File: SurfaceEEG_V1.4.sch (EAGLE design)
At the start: 69 parts, among them IC1 LMV602, IC2 TSZ124IQ4T, U1 MCP4442-103E/ST, U2 ATMEGA328P-MU

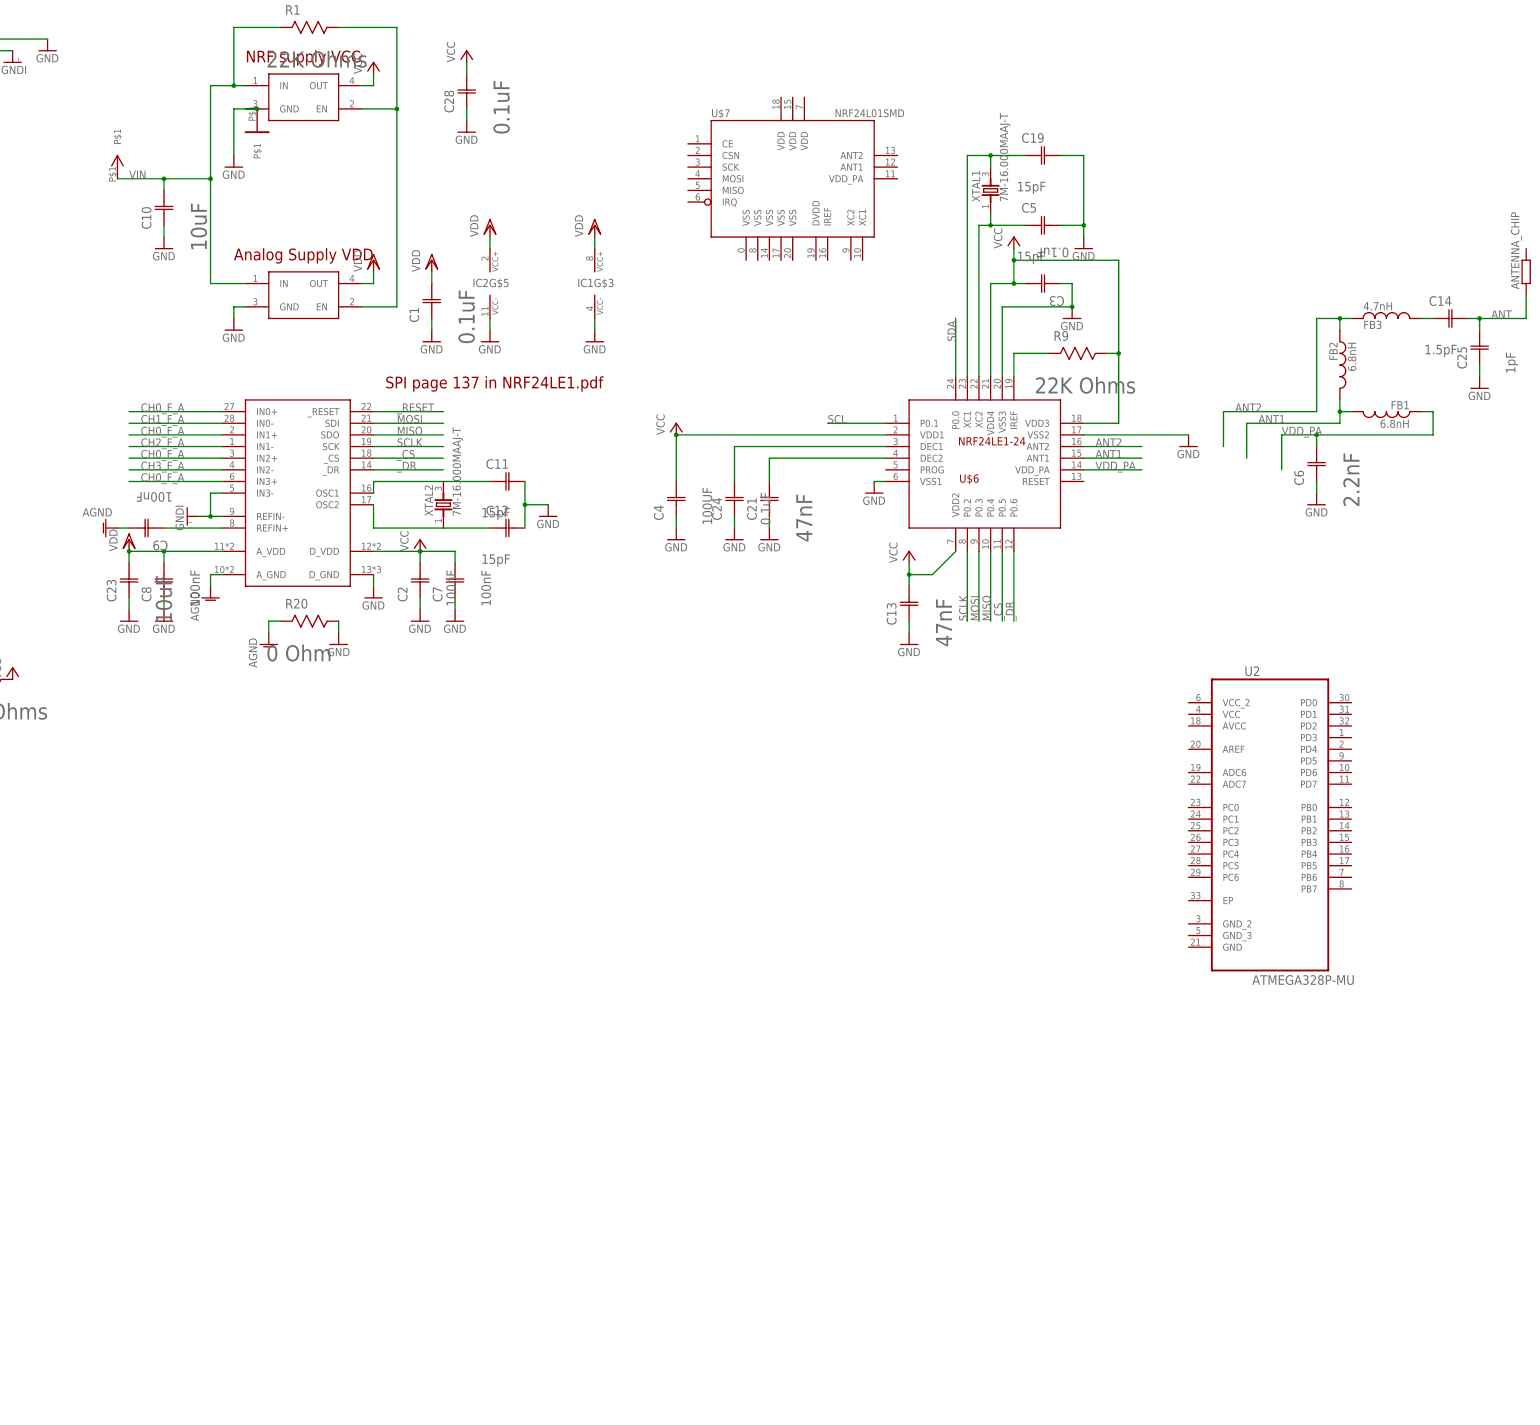
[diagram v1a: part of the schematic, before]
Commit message: Version 1.4 with atmega328 and hrf24L01 ready
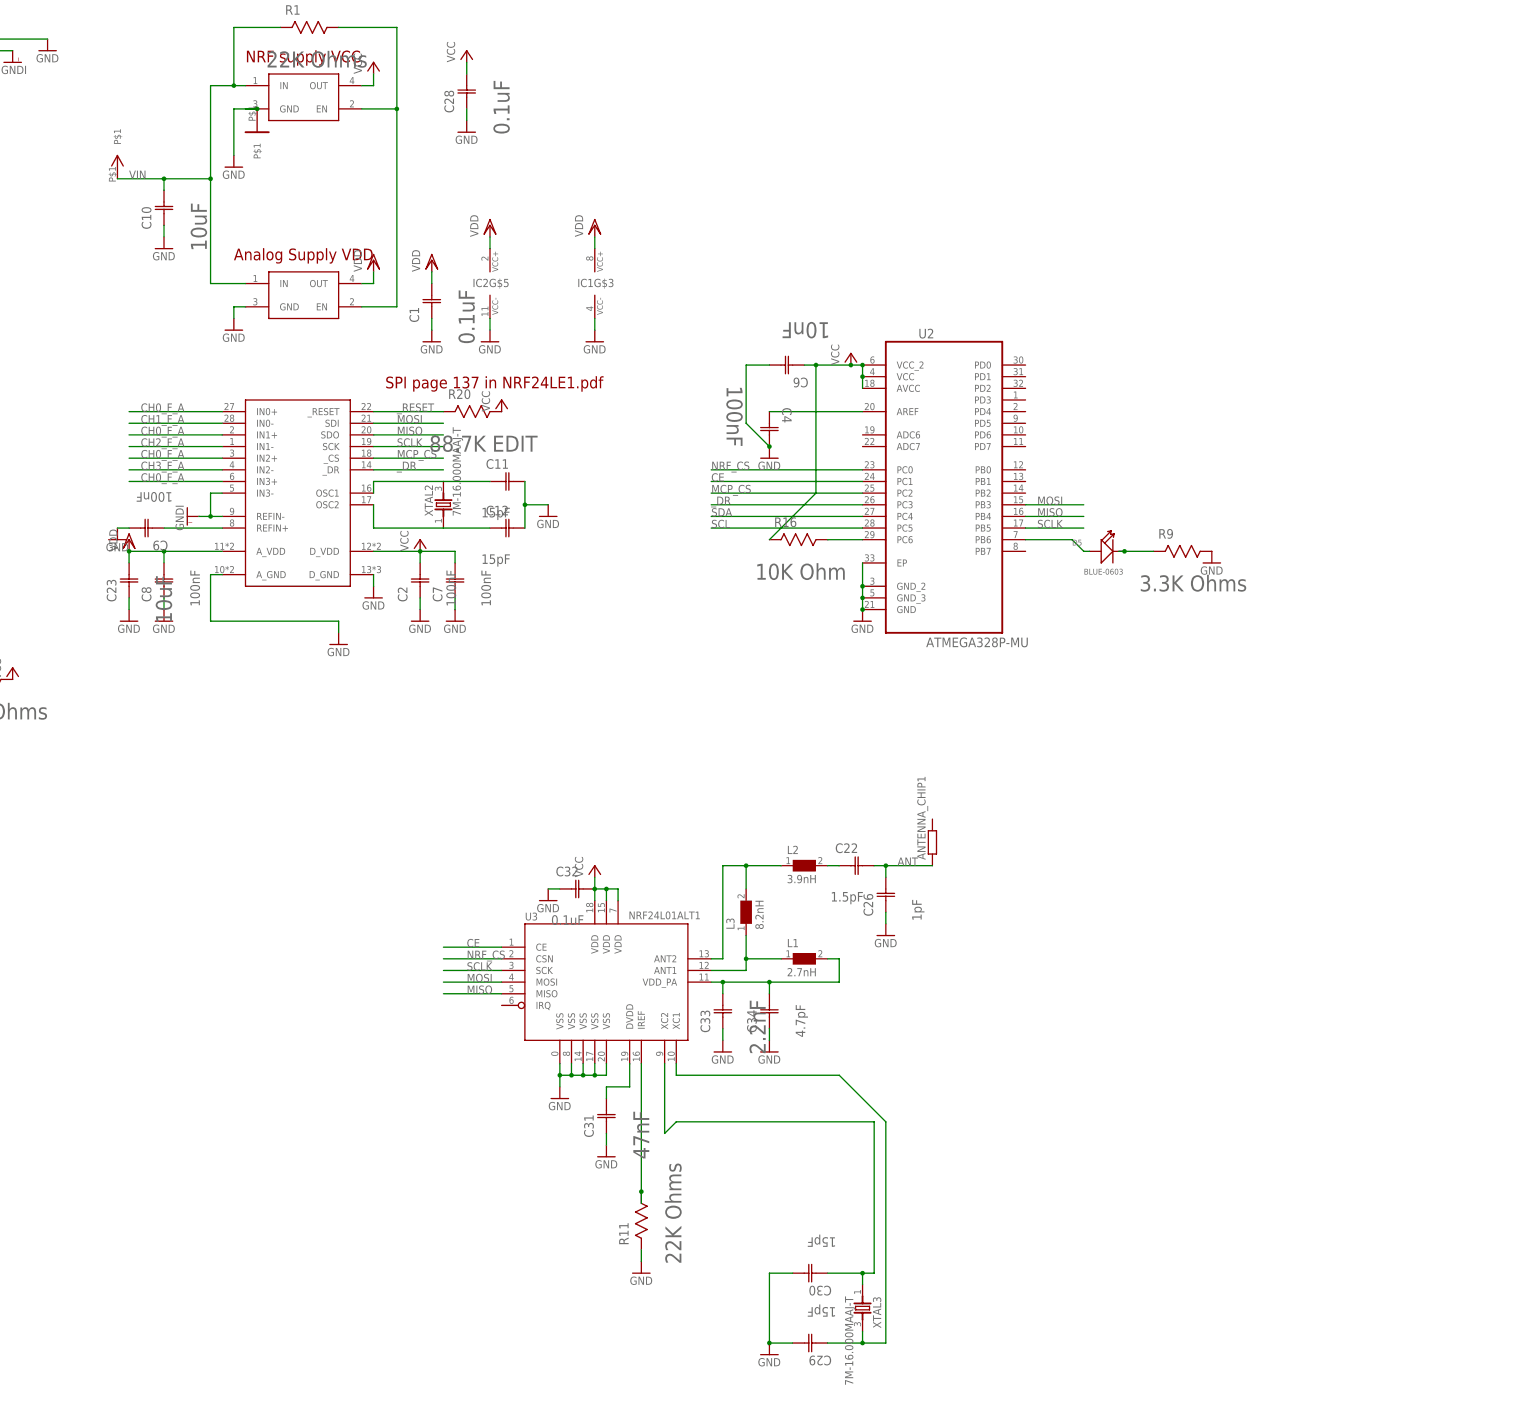
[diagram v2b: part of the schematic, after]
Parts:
- removed ANTENNA_CHIP: (no value), ELL-i-Passives:R0805
- removed C13, C21: 47nF, (manufact)-Kemet-element14:C0603C473K1RACTU
- removed C14: 1.5pF, (manufact)-capacitors-AVX-element14:UQCL2A1R5BAT2A/500
- removed C19, C5: 15pF, (manufact)-capacitors-AVX-element14:UQCL2A150JAT2A/500
- removed C24, C3: 0.1uF, (manufact)-capacitors-AVX-element14:04023C104KAT2A
- removed C25: 1pF, (manufact)-capacitors-AVX-element14:UQCL2A1R0BAT2A/500
- removed FB1, FB2: 6.8nH, ELL-i-Passives:FB0402
- removed FB3: 4.7nH, ELL-i-Passives:FB0402
- removed U$6: NRF24LE1-24, (misc)-parts-that-we-use:NRF24LE1-24
- removed U$7: NRF24L01SMD, (misc)-parts-that-we-use:NRF24L01SMD
- removed XTAL1: 7M-16.000MAAJ-T, (misc)-parts-that-we-use:7M-16.000MAAJ-T
- added ANTENNA_CHIP1: (no value), ELL-i-Passives:R0805
- added C22: 1.5pF, (manufact)-capacitors-AVX-element14:UQCL2A1R5BAT2A/500
- added C26: 1pF, (manufact)-capacitors-AVX-element14:UQCL2A1R0BAT2A/500
- added C29, C30: 15pF, (manufact)-capacitors-AVX-element14:UQCL2A150JAT2A/500
- added C31: 47nF, (manufact)-Kemet-element14:C0603C473K1RACTU
- added C32: 0.1uF, (manufact)-capacitors-AVX-element14:04023C104KAT2A
- added C33: 2.2nF, (manufact)-Kemet-element14:C0402C222K5RACTU
- added C34: 4.7pF, (manufact)-capacitors-AVX-element14:UQCL2A4R7CAT2A/500
- added D5: BLUE-0603, Seeed-OPL-Diode:SMD-LED-CLEAR-BLUE(0603)
- added L1: 2.7nH, (manufact)-inductors-WE-KI-element14:WE-KI-744765027A_0402A
- added L2: 3.9nH, (manufact)-inductors-WE-KI-element14:WE-KI-744765039A_0402A
- added L3: 8.2nH, (manufact)-inductors-WE-KI-element14:WE-KI-744765082A_0402A
- added R11: 22K Ohms, (manufact)-resistors-YAGEO-element14:RC0603FR-0722KL
- added R16: 10K Ohm, (manufact)-resistors-YAGEO-element14:9C06031A1002JLHFT
- added U3: NRF24L01ALT1, Testing:NRF24L01ALT1
- added XTAL3: 7M-16.000MAAJ-T, (misc)-parts-that-we-use:7M-16.000MAAJ-T
- C4: value 100UF -> 100nF; device (manufact)-capacitors-AVX-element14:1206YD106MAT2A -> (manufact)-Kemet-element14:C0603C104K4RACTU
- C6: value 2.2nF -> 10nF; device (manufact)-Kemet-element14:C0402C222K5RACTU -> (manufact)-Kemet-element14:C0603C103J3GACTU
- R20: value 0 Ohm -> 88.7K EDIT; device (manufact)-resistors-YAGEO-element14:9C06031A0R00JLHFT -> (manufact)-resistors-YAGEO-element14:RT0603FRE0782KL
- R9: value 22K Ohms -> 3.3K Ohms; device (manufact)-resistors-YAGEO-element14:RC0603FR-0722KL -> (manufact)-resistors-YAGEO-element14:RC0603FR-073K3L
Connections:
- removed net AGND: C9.C2, R20.R2, U$3.A_GND
- removed net N$10: C5.C1, U$6.XC2, XTAL1.1
- removed net N$11: C19.C1, U$6.XC1, XTAL1.3
- removed net N$22: C14.C1, FB3.2
- removed net N$3: C21.C2, U$6.DEC2
- removed net VDD_PA: C6.C2, FB1.1, U$6.VDD_PA
- removed net _CS: U$3._CS, U$6.P0.5
- new net CE: U2.PC1, U3.CE
- new net MCP_CS: U$3._CS, U2.PC2
- new net N$13: C22.C1, L2.2
- new net N$16: C33.C2, C34.C2, L1.2, U3.VDD_PA
- new net N$19: R11.R1, U3.IREF
- new net N$20: C31.C2, U3.DVDD
- new net N$7: C4.C1, U2.AREF
- new net N$8: C30.C1, U3.XC2, XTAL3.1
- new net N$9: C29.C1, U3.XC1, XTAL3.3
- new net NRF_CS: U2.PC0, U3.CSN
- new net RESET: R16.R1, U2.PC6
- net ANT: now also ANTENNA_CHIP1.1, C22.C2, C26.C2; no longer ANTENNA_CHIP.1, C14.C2, C25.C2
- net ANT1: now also L1.1, L3.1, U3.ANT1; no longer FB1.2, FB2.2, U$6.ANT1
- net ANT2: now also L2.1, L3.2, U3.ANT2; no longer FB2.1, FB3.1, U$6.ANT2
- net GND: now also C26.C1, C29.C2, C30.C2, C31.C1, C32.C1, C33.C1, C34.C1, C4.C2, C6.C2, C9.C2, R11.R2, R9.R1, U$3.A_GND, U2.EP, U2.GND, U2.GND_2, U2.GND_3, U3.VSS@0, U3.VSS@14, U3.VSS@17, U3.VSS@20, U3.VSS@8; no longer C13.C1, C19.C2, C21.C1, C24.C1, C25.C1, C3.C1, C4.C1, C5.C2, C6.C1, R20.R1, U$6.VSS1, U$6.VSS2, U$6.VSS3
- net MISO: now also U2.PB4, U3.MISO; no longer U$6.P0.4
- net MOSI: now also U2.PB3, U3.MOSI; no longer U$6.P0.3
- net N$1: now also D5.+, U2.PB6; no longer R9.R2, U$6.IREF
- net N$2: now also D5.-, R9.R2; no longer C24.C2, U$6.DEC1
- net SCL: now also U2.PC5; no longer U$6.P0.1
- net SCLK: now also U2.PB5, U3.SCK; no longer U$6.P0.2
- net SDA: now also U2.PC4; no longer U$6.P0.0
- net VCC: now also C32.C2, C6.C1, R16.R2, R20.R1, U2.AVCC, U2.VCC, U2.VCC_2, U3.VDD@15, U3.VDD@18, U3.VDD@7; no longer C13.C2, C3.C2, C4.C2, R9.R1, U$6.VDD1, U$6.VDD2, U$6.VDD3, U$6.VDD4
- net _DR: now also U2.PC3; no longer U$6.P0.6
- net _RESET: now also R20.R2
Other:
- moved on the sheet: C4, C6, R20, R9, U2

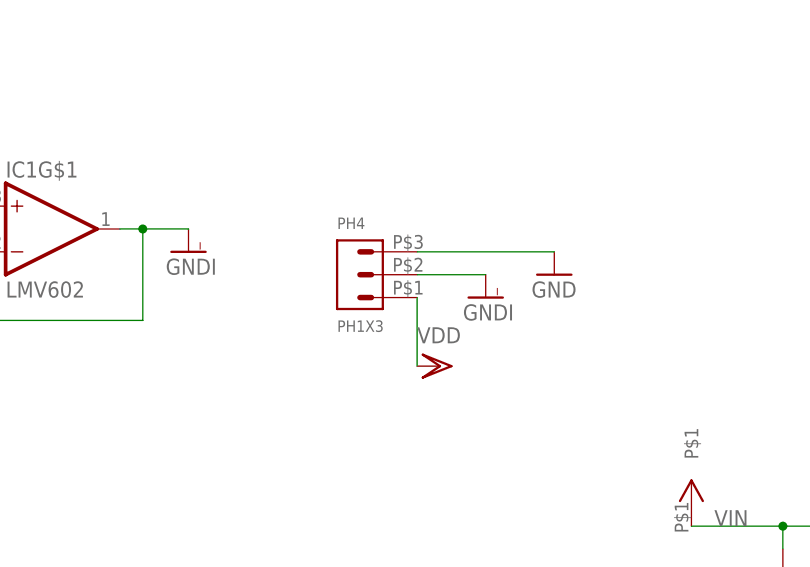
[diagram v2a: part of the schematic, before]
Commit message: Updated all boards in order to comply with DRC
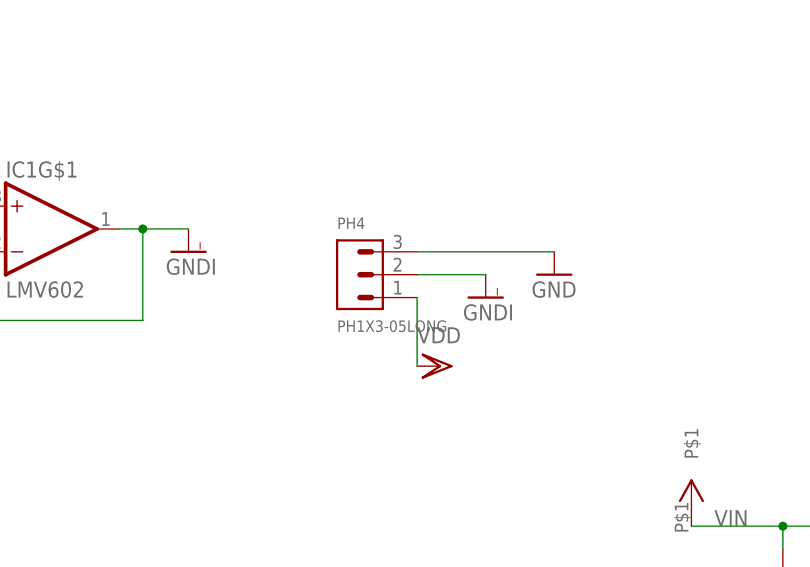
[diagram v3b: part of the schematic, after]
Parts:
- PH4: value PH1X3 -> PH1X3-05LONG; device (misc)-parts-that-we-use:PH1X3 -> (misc)-parts-that-we-use:PH1X3-05LONG
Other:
- moved on the sheet: PH4
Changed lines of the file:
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@@
 <part name="GNDI19" library="supply1" deviceset="GNDI" device=""/>
 <part name="VDD7" library="supply1" deviceset="VDD" device=""/>
-<part name="PH4" library="(misc)-parts-that-we-use" deviceset="PH1X3" device=""/>
+<part name="PH4" library="(misc)-parts-that-we-use" deviceset="PH1X3" device="-05LONG"/>
 <part name="R13" library="(manufact)-resistors-YAGEO-element14" deviceset="9C04021A4701JLHF3" device="" value="4.7K Ohms"/>
 <part name="R21" library="(manufact)-resistors-YAGEO-element14" deviceset="9C04021A4701JLHF3" device="" value="4.7K Ohms"/>

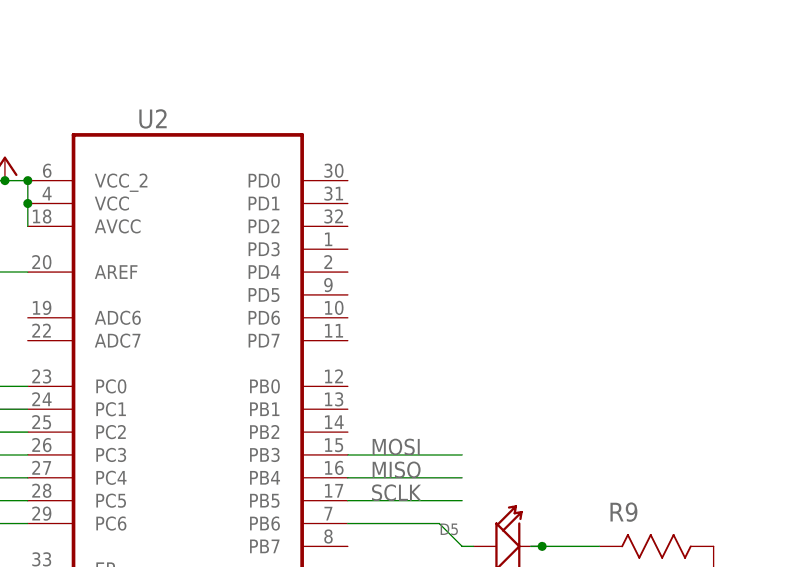
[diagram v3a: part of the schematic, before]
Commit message: added led
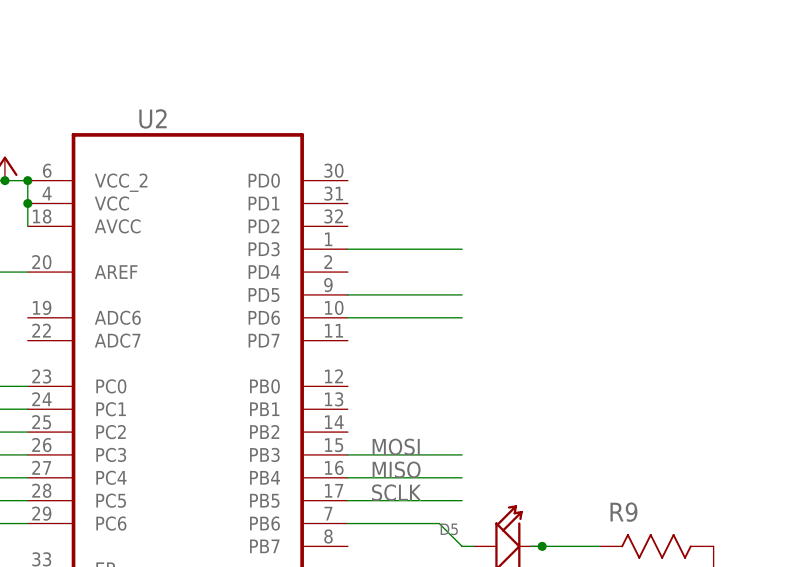
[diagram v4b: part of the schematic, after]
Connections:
- new net N$10: U2.PD6
- new net N$3: U2.PD3
- new net N$6: U2.PD5
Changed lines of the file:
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@@
+</segment>
+</net>
+<net name="N$3" class="0">
+<segment>
+<pinref part="U2" gate="A" pin="PD3"/>
+<wire x1="213.36" y1="116.84" x2="226.06" y2="116.84" width="0.1524" layer="91"/>
+</segment>
+</net>
+<net name="N$6" class="0">
+<segment>
+<pinref part="U2" gate="A" pin="PD5"/>
+<wire x1="213.36" y1="111.76" x2="226.06" y2="111.76" width="0.1524" layer="91"/>
+</segment>
+</net>
+<net name="N$10" class="0">
+<segment>
+<pinref part="U2" gate="A" pin="PD6"/>
+<wire x1="213.36" y1="109.22" x2="226.06" y2="109.22" width="0.1524" layer="91"/>
 </segment>
 </net>
